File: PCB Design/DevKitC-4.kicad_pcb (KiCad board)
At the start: 2 copper layers, 86.9 x 63.7 mm, 18 parts, among them J1 Screw_Terminal_01x02, J2 Screw_Terminal_01x02, J3 Screw_Terminal_01x04, J5 Screw_Terminal_01x03, Q1 IRFZ44N, SW1 SW_DPDT_x2, U1 ESP32-NodeMCU-32s, U2 Generic_5v_Module

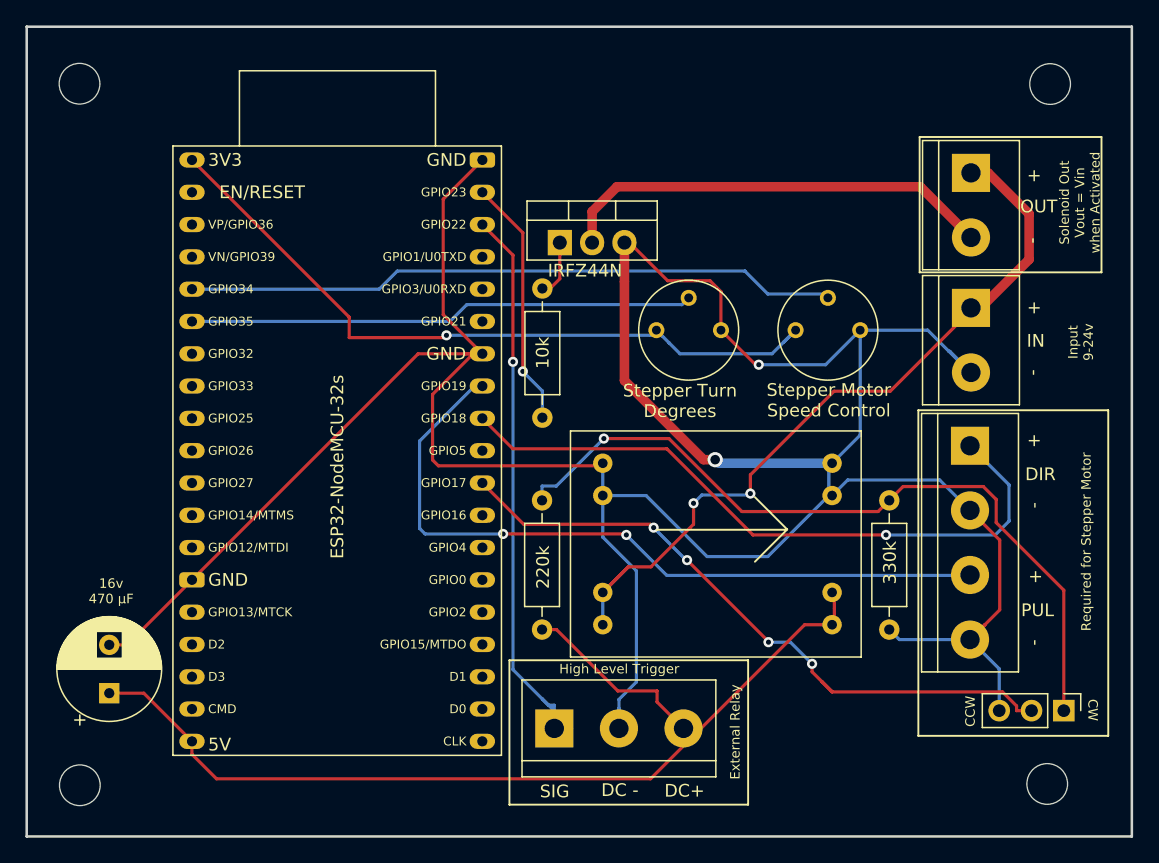
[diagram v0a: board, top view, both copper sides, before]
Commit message: modified variable names to be more self explanatory
Also changed from LOW to HIGH trigger relay options.  Added DevKitC board.
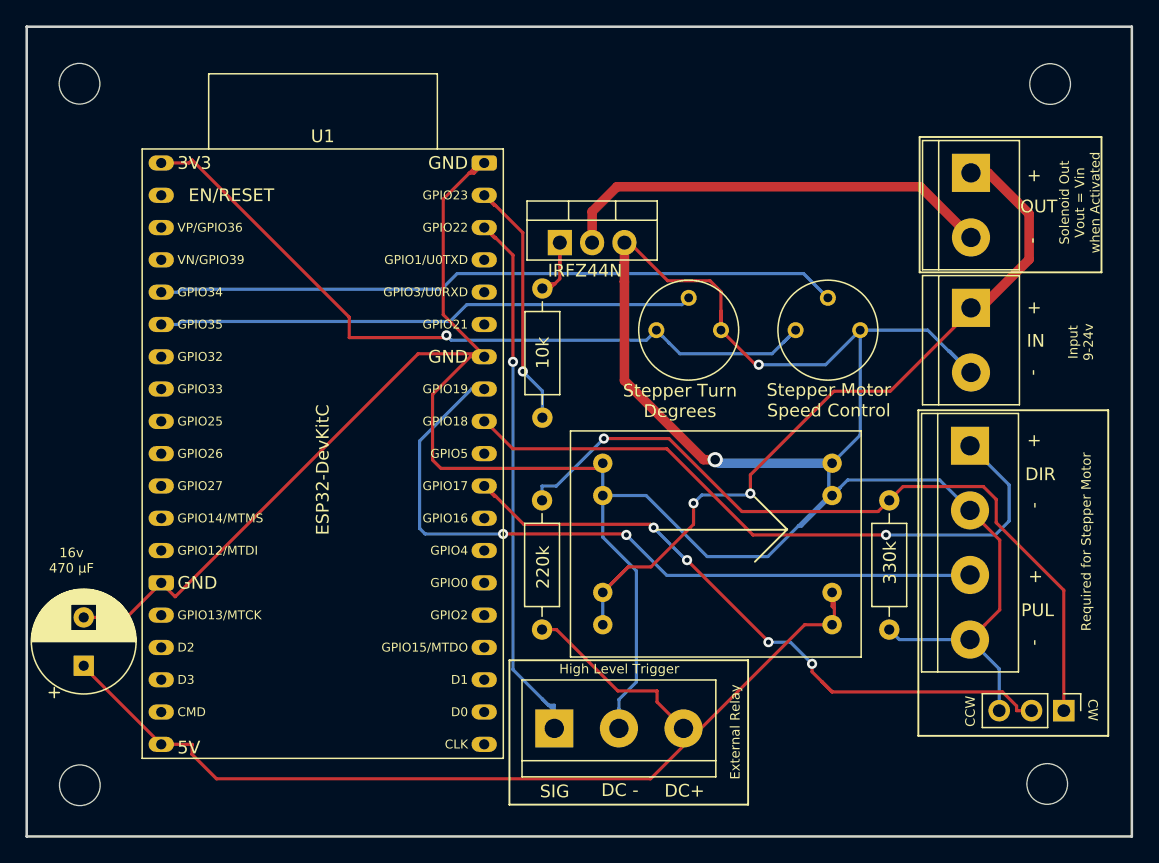
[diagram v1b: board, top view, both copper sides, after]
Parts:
- U1: value ESP32-NodeMCU-32s -> ESP32-DevKitC; footprint ESP32_modules:NodeMCU-32S -> ESP32_modules:ESP32-DevKitC
- moved C1 2.95 mm to (63.9, 100.7)
- moved U1 1.17 mm to (70.0, 61.2)
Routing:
- net +5V: track 80.5 -> 84.7 mm
- net GND: track 247.9 -> 251.9 mm
- net +3V3: track 56.6 -> 59.5 mm
- net ANGLE_POT: track 39.5 -> 42.0 mm
- net Net-(Q1-Pad1): track 3.25 -> 5.64 mm
- net SPEED_POT: track 51.0 -> 53.4 mm
- net Net-(SW1-Pad2): track 52.3 -> 53.6 mm
- net highActivationPin: track 19.7 -> 20.9 mm
- net PUL: track 57.8 -> 58.8 mm
- net VCC: track 60.1 -> 59.4 mm

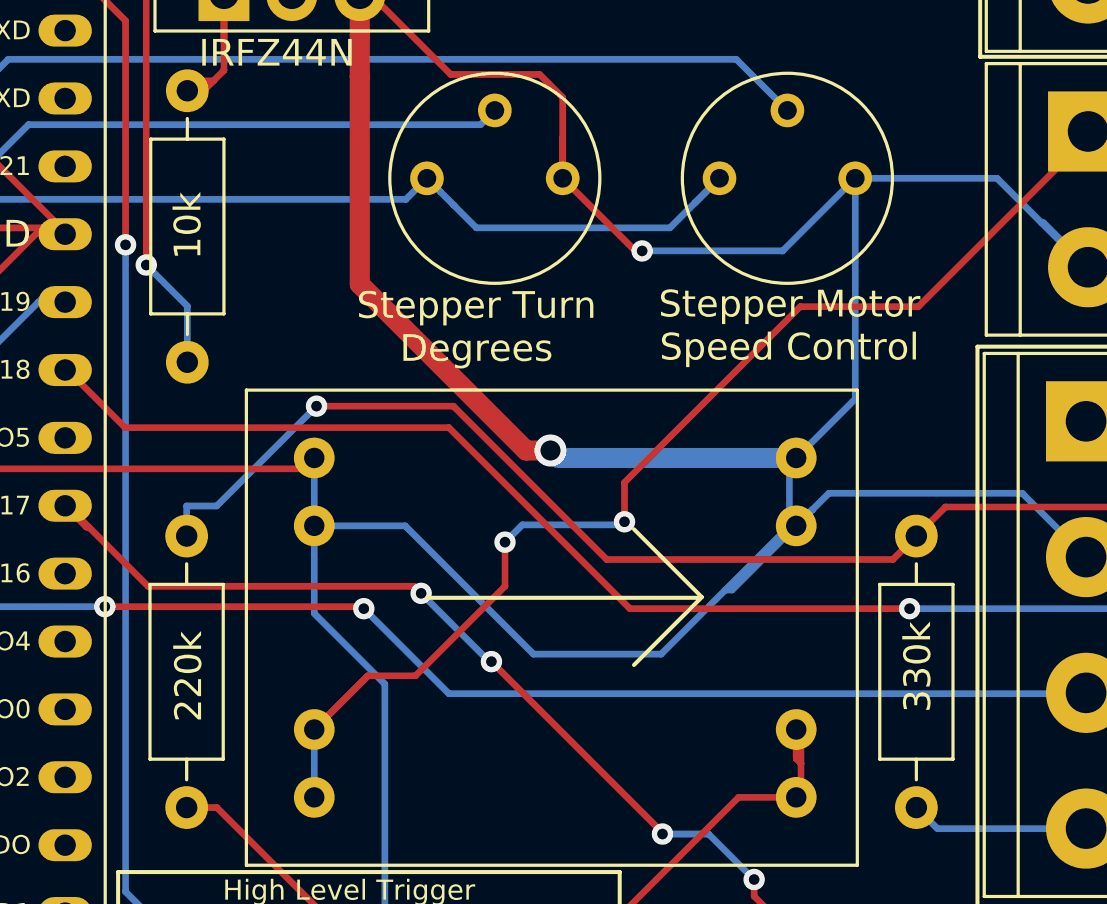
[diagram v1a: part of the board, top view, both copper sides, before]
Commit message: corrected PCB symbols
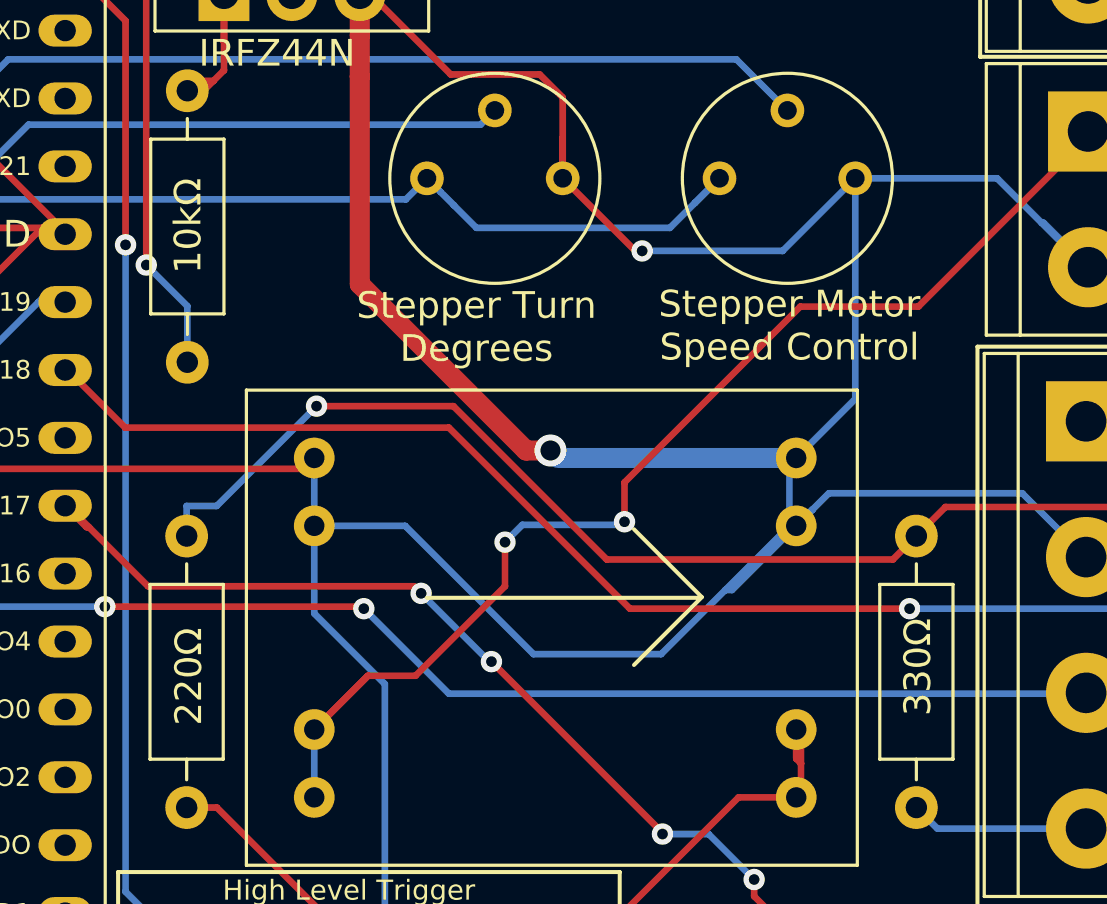
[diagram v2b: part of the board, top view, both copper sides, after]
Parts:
- R1: value 10k -> 10kΩ
- R3: value 220k -> 220Ω
- R4: value 330k -> 330Ω
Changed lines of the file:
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@@
       (effects (font (size 1 1) (thickness 0.15)))
     )
-    (fp_text value "330k" (at 4.9022 -0.0508 90) (layer "F.SilkS")
+    (fp_text value "330Ω" (at 4.9022 -0.0508 90) (layer "F.SilkS")
       (effects (font (size 1 1) (thickness 0.15)))
     )
@@
       (effects (font (size 1 1) (thickness 0.15)))
     )
-    (fp_text value "10k" (at 5.1054 0.0254 90) (layer "F.SilkS")
+    (fp_text value "10kΩ" (at 5.1054 0.0254 90) (layer "F.SilkS")
       (effects (font (size 1 1) (thickness 0.15)))
     )
@@
       (effects (font (size 1 1) (thickness 0.15)))
     )
-    (fp_text value "220k" (at 4.9022 0.0762 90) (layer "F.SilkS")
-      (effects (font (size 1 1) (thickness 0.15)))
-    )
+    (fp_text value "220Ω" (at 4.9022 0.0762 90) (layer "F.SilkS")
+      (effects (font (size 1 1) (thickness 0.15)))
+    )

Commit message: slight DC buck converter change
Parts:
- moved H1 0.19 mm to (139.7, 110.2)
- moved H4 0.10 mm to (139.8, 55.0)
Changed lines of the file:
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@@
       (effects (font (size 1 1) (thickness 0.15)))
     )
+    (fp_line (start -12.7 7.62) (end -12.7 -10.16) (layer "F.SilkS") (width 0.12))
+    (fp_line (start 10.16 7.62) (end -12.7 7.62) (layer "F.SilkS") (width 0.12))
     (fp_line (start 10.16 -10.16) (end 10.16 7.62) (layer "F.SilkS") (width 0.12))
     (fp_line (start -12.7 -10.16) (end 10.16 -10.16) (layer "F.SilkS") (width 0.12))
-    (fp_line (start -12.7 7.62) (end -12.7 -10.16) (layer "F.SilkS") (width 0.12))
-    (fp_line (start 10.16 7.62) (end -12.7 7.62) (layer "F.SilkS") (width 0.12))
-    (pad "1" thru_hole circle (at -10.16 -5.08) (size 1.524 1.524) (drill 0.762) (layers *.Cu *.Mask)
+    (pad "1" thru_hole circle (at -10.414 -7.62) (size 1.524 1.524) (drill 0.762) (layers *.Cu *.Mask)
       (net 2 "GND") (pinfunction "IN-") (pintype "input"))
-    (pad "1" thru_hole circle (at -10.16 -7.62) (size 1.524 1.524) (drill 0.762) (layers *.Cu *.Mask)
+    (pad "1" thru_hole circle (at -10.414 -5.08) (size 1.524 1.524) (drill 0.762) (layers *.Cu *.Mask)
       (net 2 "GND") (pinfunction "IN-") (pintype "input"))
-    (pad "2" thru_hole circle (at -10.16 2.54) (size 1.524 1.524) (drill 0.762) (layers *.Cu *.Mask)
+    (pad "2" thru_hole circle (at -10.414 2.54) (size 1.524 1.524) (drill 0.762) (layers *.Cu *.Mask)
       (net 1 "VCC") (pinfunction "IN+") (pintype "input"))
-    (pad "2" thru_hole circle (at -10.16 5.08) (size 1.524 1.524) (drill 0.762) (layers *.Cu *.Mask)
+    (pad "2" thru_hole circle (at -10.414 5.08) (size 1.524 1.524) (drill 0.762) (layers *.Cu *.Mask)
       (net 1 "VCC") (pinfunction "IN+") (pintype "input"))
-    (pad "3" thru_hole circle (at 7.874 -7.62) (size 1.524 1.524) (drill 0.762) (layers *.Cu *.Mask)
+    (pad "3" thru_hole circle (at 8.128 -7.62) (size 1.524 1.524) (drill 0.762) (layers *.Cu *.Mask)
       (net 2 "GND") (pinfunction "5v-") (pintype "output"))
-    (pad "3" thru_hole circle (at 7.874 -5.08) (size 1.524 1.524) (drill 0.762) (layers *.Cu *.Mask)
+    (pad "3" thru_hole circle (at 8.128 -5.08) (size 1.524 1.524) (drill 0.762) (layers *.Cu *.Mask)
       (net 2 "GND") (pinfunction "5v-") (pintype "output"))
-    (pad "4" thru_hole circle (at 7.874 2.54) (size 1.524 1.524) (drill 0.762) (layers *.Cu *.Mask)
+    (pad "4" thru_hole circle (at 8.128 5.08) (size 1.524 1.524) (drill 0.762) (layers *.Cu *.Mask)
       (net 5 "+5V") (pinfunction "5v") (pintype "output"))
-    (pad "4" thru_hole circle (at 7.874 5.08) (size 1.524 1.524) (drill 0.762) (layers *.Cu *.Mask)
+    (pad "4" thru_hole circle (at 8.128 2.54) (size 1.524 1.524) (drill 0.762) (layers *.Cu *.Mask)
       (net 5 "+5V") (pinfunction "5v") (pintype "output"))
   )
@@
   )
   (footprint "MountingHole:MountingHole_3.2mm_M3" (layer "F.Cu")
-    (at 139.6492 110.0328)
+    (at 139.7254 110.2106)
     (descr "Mounting Hole 3.2mm, no annular, M3")
     (tags "mounting hole 3.2mm no annular m3")
@@
   )
   (footprint "MountingHole:MountingHole_3.2mm_M3" (layer "F.Cu")
-    (at 139.8778 54.991)
+    (at 139.7762 54.991)
     (descr "Mounting Hole 3.2mm, no annular, M3")
     (tags "mounting hole 3.2mm no annular m3")
@@
   (segment (start 135.636 89.4783) (end 140.955 94.7973) (width 0.25) (layer "F.Cu") (net 40))
   (via (at 104.784 82.8714) (size 0.8) (drill 0.4) (layers "F.Cu" "B.Cu") (net 40))
-  (segment (start 101.049 86.6065) (end 99.9236 86.6065) (width 0.25) (layer "B.Cu") (net 40))
-  (segment (start 104.784 82.8714) (end 101.049 86.6065) (width 0.25) (layer "B.Cu") (net 40))
-  (segment (start 99.9236 86.6065) (end 99.9236 87.7316) (width 0.25) (layer "B.Cu") (net 40))
+  (segment (start 104.784 82.8714) (end 103.5646 82.8714) (width 0.25) (layer "B.Cu") (net 40))
+  (segment (start 99.9236 86.5124) (end 99.9236 87.7316) (width 0.25) (layer "B.Cu") (net 40))
+  (segment (start 103.5646 82.8714) (end 99.9236 86.5124) (width 0.25) (layer "B.Cu") (net 40))
 )

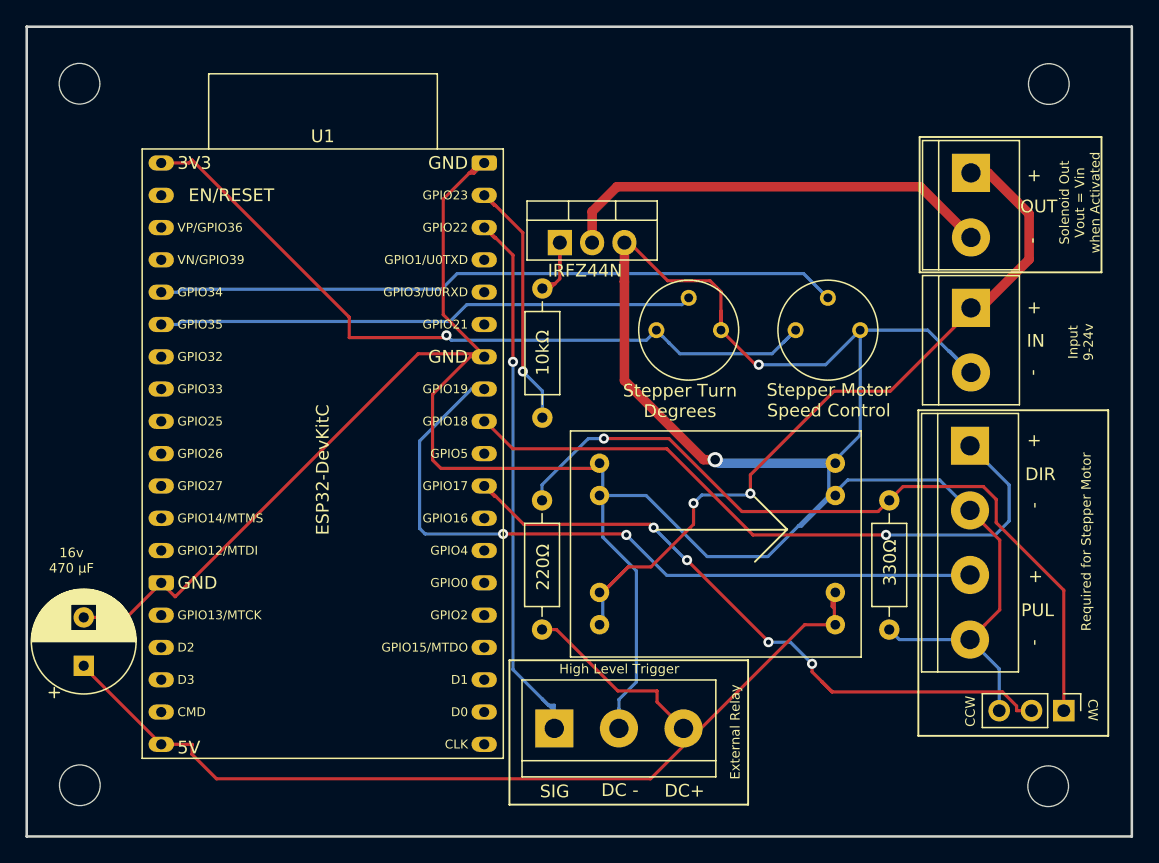
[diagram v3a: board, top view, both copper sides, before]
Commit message: drill hole changes
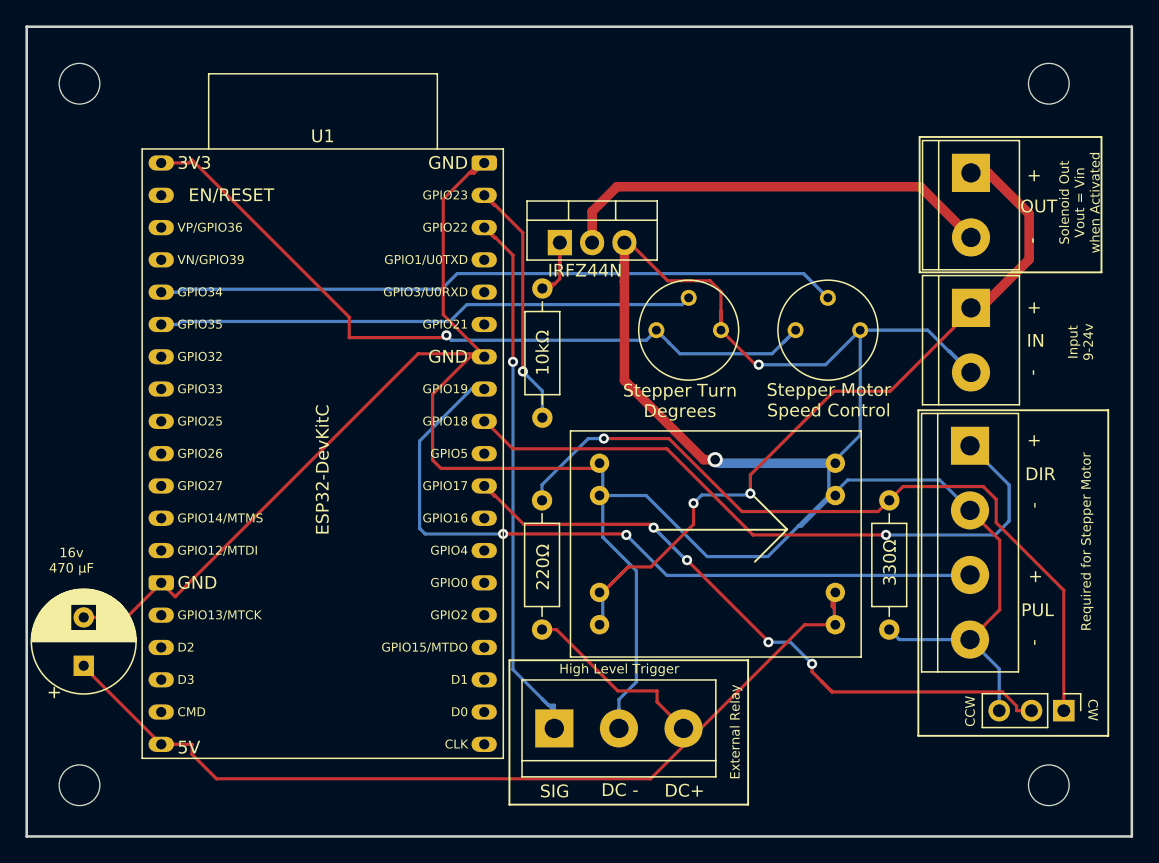
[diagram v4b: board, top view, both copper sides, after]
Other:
- board text added: "Board Design 1.9"
- board text removed: "Board Design 1.8"
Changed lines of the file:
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@@
     (fp_circle (center 0 0) (end 3.2 0) (layer "Cmts.User") (width 0.15) (fill none))
     (fp_circle (center 0 0) (end 3.45 0) (layer "F.CrtYd") (width 0.05) (fill none))
-    (pad "" np_thru_hole circle (at 0 0) (size 3.2 3.2) (drill 3.2) (layers *.Cu *.Mask))
+    (pad "" np_thru_hole circle (at 0 0) (size 3.2 3.2) (drill 3.2) (layers F&B.Cu *.Mask))
   )
   (footprint "Resistor_THT:R_Axial_DIN0207_L6.3mm_D2.5mm_P10.16mm_Horizontal" (layer "F.Cu")
@@
     (fp_circle (center 0 0) (end 3.2 0) (layer "Cmts.User") (width 0.15) (fill none))
     (fp_circle (center 0 0) (end 3.45 0) (layer "F.CrtYd") (width 0.05) (fill none))
-    (pad "" np_thru_hole circle (at 0 0) (size 3.2 3.2) (drill 3.2) (layers *.Cu *.Mask))
+    (pad "" np_thru_hole circle (at 0.0508 -0.0762) (size 3.2 3.2) (drill 3.2) (layers F&B.Cu *.Mask))
   )
   (footprint "Potentiometer_THT:Potentiometer_Bourns_3339P_Vertical" (layer "F.Cu")
@@
     (fp_circle (center 0 0) (end 3.2 0) (layer "Cmts.User") (width 0.15) (fill none))
     (fp_circle (center 0 0) (end 3.45 0) (layer "F.CrtYd") (width 0.05) (fill none))
-    (pad "" np_thru_hole circle (at 0 0) (size 3.2 3.2) (drill 3.2) (layers *.Cu *.Mask))
+    (pad "" np_thru_hole circle (at -0.0254 0) (size 3.2 3.2) (drill 3.2) (layers F&B.Cu *.Mask))
   )
   (footprint "MountingHole:MountingHole_3.2mm_M3" (layer "F.Cu")
@@
     (fp_circle (center 0 0) (end 3.2 0) (layer "Cmts.User") (width 0.15) (fill none))
     (fp_circle (center 0 0) (end 3.45 0) (layer "F.CrtYd") (width 0.05) (fill none))
-    (pad "" np_thru_hole circle (at 0 0) (size 3.2 3.2) (drill 3.2) (layers *.Cu *.Mask))
+    (pad "" np_thru_hole circle (at 0 -0.0254) (size 3.2 3.2) (drill 3.2) (layers F&B.Cu *.Mask))
   )
   (footprint "Connector_PinHeader_2.54mm:PinHeader_1x03_P2.54mm_Vertical" (layer "F.Cu")
@@
     (effects (font (size 1 1) (thickness 0.15)))
   )
-  (gr_text "Board Design 1.8\n\n\n" (at 83.82 55.88) (layer "B.SilkS")
+  (gr_text "Board Design 1.9\n\n\n" (at 83.82 55.88) (layer "B.SilkS")
     (effects (font (size 2 2) (thickness 0.25)) (justify mirror))
   )
